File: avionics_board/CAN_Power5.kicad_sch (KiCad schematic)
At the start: 4 parts, among them U10 AP3602AKTR-G1

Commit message: create Common global libraries for footprints and symbols
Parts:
- U10: footprint SOT-23-6_DIO -> Package_TO_SOT_SMD:SOT-23-6_Handsoldering
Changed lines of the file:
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@@
 			)
 		)
-		(property "Footprint" "SOT-23-6_DIO"
+		(property "Footprint" "Package_TO_SOT_SMD:SOT-23-6_Handsoldering"
 			(at 139.065 95.25 0)
 			(effects

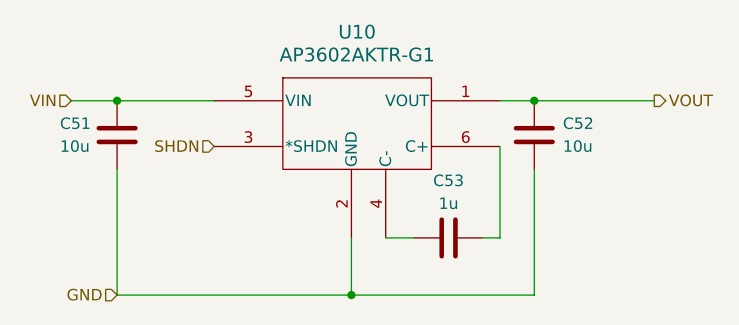
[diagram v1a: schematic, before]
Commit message: push PC104 bus reorder (no more 5V, 20 lines of 3V3 and 4 switched batt) to system components
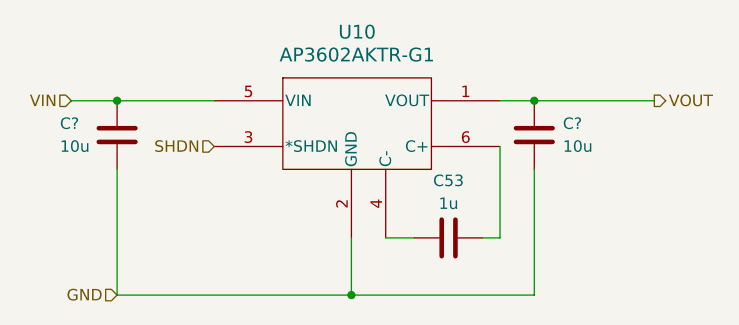
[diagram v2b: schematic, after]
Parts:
- renumbered C51 to C?, C52 to C?
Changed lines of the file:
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@@
 			(project ""
 				(path "/f6cc00ab-17f1-4973-862f-7ac95fe70668/00000000-0000-0000-0000-00005ea31c93/c43e73ca-9c1e-4d37-880f-a2757d61b5eb"
-					(reference "C52")
+					(reference "C54")
 					(unit 1)
 				)
@@
 		(on_board yes)
 		(dnp no)
-		(property "Reference" "C51"
+		(property "Reference" "C?"
 			(at 121.92 97.79 0)
 			(effects
@@
 		)
 		(instances
-			(project "sci_board"
+			(project "openlst-hw"
 				(path "/a863a5ec-a5d4-4f54-be53-e8c01d5e3ac4/53f12969-e593-459a-9671-cc23a5a9aea0/9886b2ec-bcf1-45d3-b809-b13147854a63"
-					(reference "C51")
+					(reference "C?")
 					(unit 1)
 				)
@@
 			(project "AVIONICS_BOARD"
 				(path "/f6cc00ab-17f1-4973-862f-7ac95fe70668/00000000-0000-0000-0000-00005ea31c93/c43e73ca-9c1e-4d37-880f-a2757d61b5eb"
-					(reference "C50")
+					(reference "C52")
 					(unit 1)
 				)
@@
 		(dnp no)
 		(fields_autoplaced yes)
-		(property "Reference" "C52"
+		(property "Reference" "C?"
 			(at 177.8 97.7899 0)
 			(effects
@@
 		)
 		(instances
-			(project "sci_board"
+			(project "openlst-hw"
 				(path "/a863a5ec-a5d4-4f54-be53-e8c01d5e3ac4/53f12969-e593-459a-9671-cc23a5a9aea0/9886b2ec-bcf1-45d3-b809-b13147854a63"
-					(reference "C52")
+					(reference "C?")
 					(unit 1)
 				)
@@
 			(project "AVIONICS_BOARD"
 				(path "/f6cc00ab-17f1-4973-862f-7ac95fe70668/00000000-0000-0000-0000-00005ea31c93/c43e73ca-9c1e-4d37-880f-a2757d61b5eb"
-					(reference "C51")
-					(unit 1)
-				)
+					(reference "C53")
+					(unit 1)
+				)

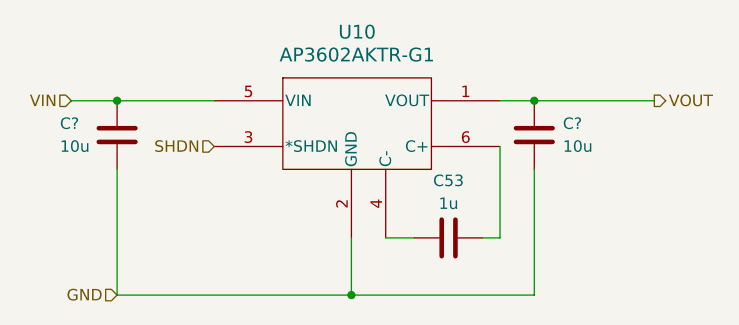
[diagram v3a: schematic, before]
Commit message: assign can power to core powerm will need to use GPIO to enable power stndby from MCUs, finalize pc104 bus assignments
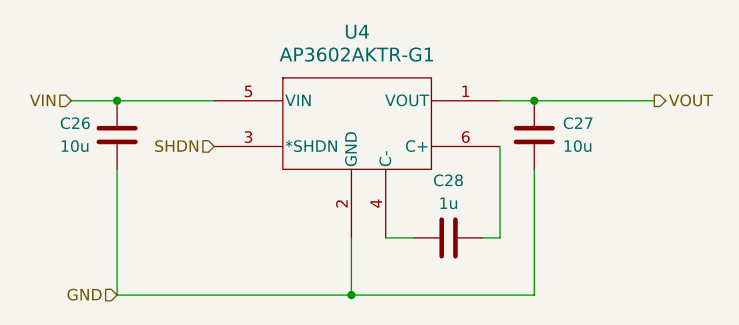
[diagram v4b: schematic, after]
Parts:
- gave numbers to parts that had none: 2
- renumbered C53 to C28, U10 to U4
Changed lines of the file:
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@@
 		(on_board yes)
 		(dnp no)
-		(property "Reference" "C53"
+		(property "Reference" "C28"
 			(at 165.1 104.14 90)
 			(effects
@@
 		)
 		(instances
-			(project ""
-				(path "/a863a5ec-a5d4-4f54-be53-e8c01d5e3ac4/53f12969-e593-459a-9671-cc23a5a9aea0/9886b2ec-bcf1-45d3-b809-b13147854a63"
-					(reference "C53")
-					(unit 1)
-				)
-			)
-			(project ""
+			(project "sci_board"
 				(path "/b4b2c88d-f6cd-4e60-862d-e21f68728580/6cda4f26-4bfa-410a-8807-c465392c7a5e"
 					(reference "C28")
@@
 				(path "/f6cc00ab-17f1-4973-862f-7ac95fe70668/00000000-0000-0000-0000-00005ea31c93/c43e73ca-9c1e-4d37-880f-a2757d61b5eb"
 					(reference "C54")
+					(unit 1)
+				)
+				(path "/f6cc00ab-17f1-4973-862f-7ac95fe70668/00000000-0000-0000-0000-00005ea31c93/00000000-0000-0000-0000-00005eab1057/c7f59f71-76ca-408f-9d9f-2fe019860d6e"
+					(reference "C62")
 					(unit 1)
 				)
@@
 		(on_board yes)
 		(dnp no)
-		(property "Reference" "C?"
+		(property "Reference" "C26"
 			(at 121.92 97.79 0)
 			(effects
@@
 		)
 		(instances
-			(project "openlst-hw"
-				(path "/a863a5ec-a5d4-4f54-be53-e8c01d5e3ac4/53f12969-e593-459a-9671-cc23a5a9aea0/9886b2ec-bcf1-45d3-b809-b13147854a63"
-					(reference "C?")
-					(unit 1)
-				)
-			)
 			(project "sci_board"
 				(path "/b4b2c88d-f6cd-4e60-862d-e21f68728580/6cda4f26-4bfa-410a-8807-c465392c7a5e"
@@
 				(path "/f6cc00ab-17f1-4973-862f-7ac95fe70668/00000000-0000-0000-0000-00005ea31c93/c43e73ca-9c1e-4d37-880f-a2757d61b5eb"
 					(reference "C52")
+					(unit 1)
+				)
+				(path "/f6cc00ab-17f1-4973-862f-7ac95fe70668/00000000-0000-0000-0000-00005ea31c93/00000000-0000-0000-0000-00005eab1057/c7f59f71-76ca-408f-9d9f-2fe019860d6e"
+					(reference "C60")
 					(unit 1)
 				)
@@
 		(dnp no)
 		(fields_autoplaced yes)
-		(property "Reference" "U10"
+		(property "Reference" "U4"
 			(at 154.94 87.63 0)
 			(effects
@@
 		)
 		(instances
-			(project ""
-				(path "/a863a5ec-a5d4-4f54-be53-e8c01d5e3ac4/53f12969-e593-459a-9671-cc23a5a9aea0/9886b2ec-bcf1-45d3-b809-b13147854a63"
-					(reference "U10")
-					(unit 1)
-				)
-			)
-			(project ""
+			(project "sci_board"
 				(path "/b4b2c88d-f6cd-4e60-862d-e21f68728580/6cda4f26-4bfa-410a-8807-c465392c7a5e"
 					(reference "U4")
@@
 				(path "/f6cc00ab-17f1-4973-862f-7ac95fe70668/00000000-0000-0000-0000-00005ea31c93/c43e73ca-9c1e-4d37-880f-a2757d61b5eb"
 					(reference "U13")
+					(unit 1)
+				)
+				(path "/f6cc00ab-17f1-4973-862f-7ac95fe70668/00000000-0000-0000-0000-00005ea31c93/00000000-0000-0000-0000-00005eab1057/c7f59f71-76ca-408f-9d9f-2fe019860d6e"
+					(reference "U18")
 					(unit 1)
 				)
@@
 		(dnp no)
 		(fields_autoplaced yes)
-		(property "Reference" "C?"
+		(property "Reference" "C27"
 			(at 177.8 97.7899 0)
 			(effects
@@
 		)
 		(instances
-			(project "openlst-hw"
-				(path "/a863a5ec-a5d4-4f54-be53-e8c01d5e3ac4/53f12969-e593-459a-9671-cc23a5a9aea0/9886b2ec-bcf1-45d3-b809-b13147854a63"
-					(reference "C?")
-					(unit 1)
-				)
-			)
 			(project "sci_board"
 				(path "/b4b2c88d-f6cd-4e60-862d-e21f68728580/6cda4f26-4bfa-410a-8807-c465392c7a5e"
@@
 					(unit 1)
 				)
+				(path "/f6cc00ab-17f1-4973-862f-7ac95fe70668/00000000-0000-0000-0000-00005ea31c93/00000000-0000-0000-0000-00005eab1057/c7f59f71-76ca-408f-9d9f-2fe019860d6e"
+					(reference "C61")
+					(unit 1)
+				)

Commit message: openlst board
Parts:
- renumbered C26 to C51, C27 to C52, C28 to C53, U4 to U10
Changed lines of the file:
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@@
 		(on_board yes)
 		(dnp no)
-		(property "Reference" "C28"
+		(property "Reference" "C53"
 			(at 165.1 104.14 90)
 			(effects
@@
 		)
 		(instances
+			(project "openlst-hw"
+				(path "/a863a5ec-a5d4-4f54-be53-e8c01d5e3ac4/53f12969-e593-459a-9671-cc23a5a9aea0/9886b2ec-bcf1-45d3-b809-b13147854a63"
+					(reference "C53")
+					(unit 1)
+				)
+			)
 			(project "sci_board"
 				(path "/b4b2c88d-f6cd-4e60-862d-e21f68728580/6cda4f26-4bfa-410a-8807-c465392c7a5e"
@@
 		(on_board yes)
 		(dnp no)
-		(property "Reference" "C26"
+		(property "Reference" "C51"
 			(at 121.92 97.79 0)
 			(effects
@@
 		)
 		(instances
+			(project "openlst-hw"
+				(path "/a863a5ec-a5d4-4f54-be53-e8c01d5e3ac4/53f12969-e593-459a-9671-cc23a5a9aea0/9886b2ec-bcf1-45d3-b809-b13147854a63"
+					(reference "C51")
+					(unit 1)
+				)
+			)
 			(project "sci_board"
 				(path "/b4b2c88d-f6cd-4e60-862d-e21f68728580/6cda4f26-4bfa-410a-8807-c465392c7a5e"
@@
 		(dnp no)
 		(fields_autoplaced yes)
-		(property "Reference" "U4"
+		(property "Reference" "U10"
 			(at 154.94 87.63 0)
 			(effects
@@
 		)
 		(instances
+			(project "openlst-hw"
+				(path "/a863a5ec-a5d4-4f54-be53-e8c01d5e3ac4/53f12969-e593-459a-9671-cc23a5a9aea0/9886b2ec-bcf1-45d3-b809-b13147854a63"
+					(reference "U10")
+					(unit 1)
+				)
+			)
 			(project "sci_board"
 				(path "/b4b2c88d-f6cd-4e60-862d-e21f68728580/6cda4f26-4bfa-410a-8807-c465392c7a5e"
@@
 		(dnp no)
 		(fields_autoplaced yes)
-		(property "Reference" "C27"
+		(property "Reference" "C52"
 			(at 177.8 97.7899 0)
 			(effects
@@
 		)
 		(instances
+			(project "openlst-hw"
+				(path "/a863a5ec-a5d4-4f54-be53-e8c01d5e3ac4/53f12969-e593-459a-9671-cc23a5a9aea0/9886b2ec-bcf1-45d3-b809-b13147854a63"
+					(reference "C52")
+					(unit 1)
+				)
+			)
 			(project "sci_board"
 				(path "/b4b2c88d-f6cd-4e60-862d-e21f68728580/6cda4f26-4bfa-410a-8807-c465392c7a5e"

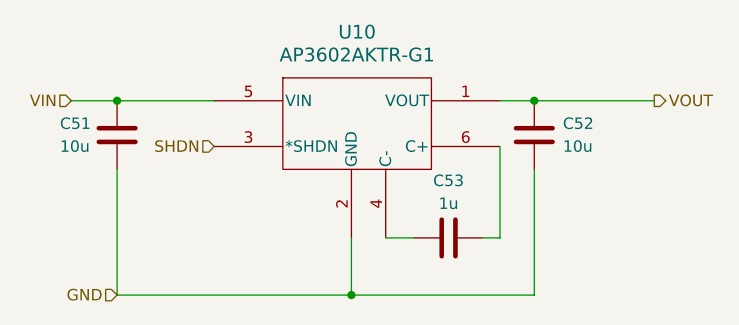
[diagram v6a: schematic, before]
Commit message: refactor AVI into nicer hierarchical components
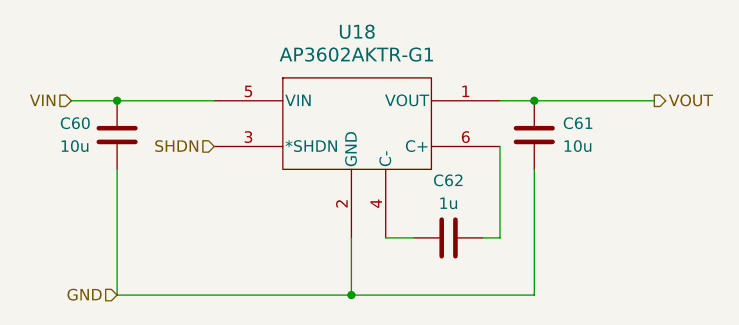
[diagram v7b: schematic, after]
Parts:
- renumbered C51 to C60, C52 to C61, C53 to C62, U10 to U18
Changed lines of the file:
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@@
 		(on_board yes)
 		(dnp no)
-		(property "Reference" "C53"
+		(property "Reference" "C62"
 			(at 165.1 104.14 90)
 			(effects
@@
 		)
 		(instances
-			(project "openlst-hw"
-				(path "/a863a5ec-a5d4-4f54-be53-e8c01d5e3ac4/53f12969-e593-459a-9671-cc23a5a9aea0/9886b2ec-bcf1-45d3-b809-b13147854a63"
-					(reference "C53")
-					(unit 1)
-				)
-			)
-			(project "sci_board"
-				(path "/b4b2c88d-f6cd-4e60-862d-e21f68728580/6cda4f26-4bfa-410a-8807-c465392c7a5e"
-					(reference "C28")
-					(unit 1)
-				)
-			)
-			(project ""
-				(path "/f6cc00ab-17f1-4973-862f-7ac95fe70668/00000000-0000-0000-0000-00005ea31c93/00000000-0000-0000-0000-00005eab1057/c7f59f71-76ca-408f-9d9f-2fe019860d6e"
+			(project "AVIONICS_BOARD"
+				(path "/f6cc00ab-17f1-4973-862f-7ac95fe70668/5de22591-2293-4710-b038-9e93720cba0f/c7f59f71-76ca-408f-9d9f-2fe019860d6e"
 					(reference "C62")
 					(unit 1)
@@
 		(on_board yes)
 		(dnp no)
-		(property "Reference" "C51"
+		(property "Reference" "C60"
 			(at 121.92 97.79 0)
 			(effects
@@
 		)
 		(instances
-			(project "openlst-hw"
-				(path "/a863a5ec-a5d4-4f54-be53-e8c01d5e3ac4/53f12969-e593-459a-9671-cc23a5a9aea0/9886b2ec-bcf1-45d3-b809-b13147854a63"
-					(reference "C51")
-					(unit 1)
-				)
-			)
-			(project "sci_board"
-				(path "/b4b2c88d-f6cd-4e60-862d-e21f68728580/6cda4f26-4bfa-410a-8807-c465392c7a5e"
-					(reference "C26")
-					(unit 1)
-				)
-			)
-			(project "AVIONICS_BOARD"
-				(path "/f6cc00ab-17f1-4973-862f-7ac95fe70668/00000000-0000-0000-0000-00005ea31c93/00000000-0000-0000-0000-00005eab1057/c7f59f71-76ca-408f-9d9f-2fe019860d6e"
+			(project "AVIONICS_BOARD"
+				(path "/f6cc00ab-17f1-4973-862f-7ac95fe70668/5de22591-2293-4710-b038-9e93720cba0f/c7f59f71-76ca-408f-9d9f-2fe019860d6e"
 					(reference "C60")
 					(unit 1)
@@
 		(dnp no)
 		(fields_autoplaced yes)
-		(property "Reference" "U10"
+		(property "Reference" "U18"
 			(at 154.94 87.63 0)
 			(effects
@@
 		)
 		(instances
-			(project "openlst-hw"
-				(path "/a863a5ec-a5d4-4f54-be53-e8c01d5e3ac4/53f12969-e593-459a-9671-cc23a5a9aea0/9886b2ec-bcf1-45d3-b809-b13147854a63"
-					(reference "U10")
-					(unit 1)
-				)
-			)
-			(project "sci_board"
-				(path "/b4b2c88d-f6cd-4e60-862d-e21f68728580/6cda4f26-4bfa-410a-8807-c465392c7a5e"
-					(reference "U4")
-					(unit 1)
-				)
-			)
-			(project ""
-				(path "/f6cc00ab-17f1-4973-862f-7ac95fe70668/00000000-0000-0000-0000-00005ea31c93/00000000-0000-0000-0000-00005eab1057/c7f59f71-76ca-408f-9d9f-2fe019860d6e"
+			(project "AVIONICS_BOARD"
+				(path "/f6cc00ab-17f1-4973-862f-7ac95fe70668/5de22591-2293-4710-b038-9e93720cba0f/c7f59f71-76ca-408f-9d9f-2fe019860d6e"
 					(reference "U18")
 					(unit 1)
@@
 		(dnp no)
 		(fields_autoplaced yes)
-		(property "Reference" "C52"
+		(property "Reference" "C61"
 			(at 177.8 97.7899 0)
 			(effects
@@
 		)
 		(instances
-			(project "openlst-hw"
-				(path "/a863a5ec-a5d4-4f54-be53-e8c01d5e3ac4/53f12969-e593-459a-9671-cc23a5a9aea0/9886b2ec-bcf1-45d3-b809-b13147854a63"
-					(reference "C52")
-					(unit 1)
-				)
-			)
-			(project "sci_board"
-				(path "/b4b2c88d-f6cd-4e60-862d-e21f68728580/6cda4f26-4bfa-410a-8807-c465392c7a5e"
-					(reference "C27")
-					(unit 1)
-				)
-			)
-			(project "AVIONICS_BOARD"
-				(path "/f6cc00ab-17f1-4973-862f-7ac95fe70668/00000000-0000-0000-0000-00005ea31c93/00000000-0000-0000-0000-00005eab1057/c7f59f71-76ca-408f-9d9f-2fe019860d6e"
+			(project "AVIONICS_BOARD"
+				(path "/f6cc00ab-17f1-4973-862f-7ac95fe70668/5de22591-2293-4710-b038-9e93720cba0f/c7f59f71-76ca-408f-9d9f-2fe019860d6e"
 					(reference "C61")
 					(unit 1)

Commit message: reconcile BOMS for AVI. SCI and AUX
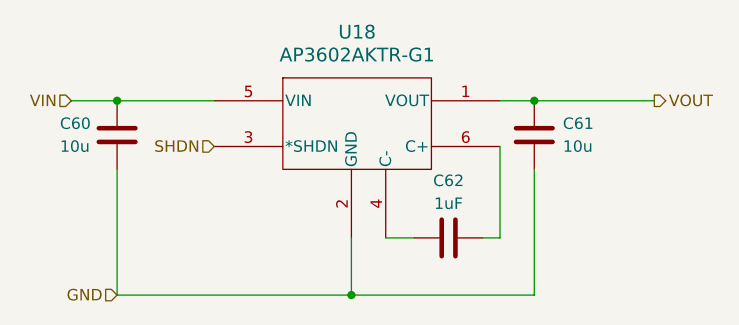
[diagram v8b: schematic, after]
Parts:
- C60, C61: Manufacturer (none) -> Murata; Part Number (none) -> GRM188R61E106KA73D; Tolerance (none) -> 10; Voltage (none) -> 25
- C62: value 1u -> 1uF; Manufacturer (none) -> Murata; Part Number (none) -> GRM188R61C105KA12D; Tolerance (none) -> 10; Voltage (none) -> 16
- U18: Manufacturer (none) -> Diodes; Part Number (none) -> AP3602AKTR-G1
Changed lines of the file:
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@@
 			)
 		)
-		(property "Value" "1u"
+		(property "Value" "1uF"
 			(at 165.1 106.68 90)
 			(effects
@@
 			)
 		)
-		(property "Datasheet" "~"
+		(property "Datasheet" "https://search.murata.co.jp/Ceramy/image/img/A01X/G101/ENG/GRM188R61C105KA12-01.pdf"
 			(at 165.1 110.49 0)
 			(effects
@@
 		)
 		(property "Alt" ""
+			(at 165.1 110.49 0)
+			(effects
+				(font
+					(size 1.27 1.27)
+				)
+				(hide yes)
+			)
+		)
+		(property "Manufacturer" "Murata"
+			(at 165.1 110.49 0)
+			(effects
+				(font
+					(size 1.27 1.27)
+				)
+				(hide yes)
+			)
+		)
+		(property "Part Number" "GRM188R61C105KA12D"
+			(at 165.1 110.49 0)
+			(effects
+				(font
+					(size 1.27 1.27)
+				)
+				(hide yes)
+			)
+		)
+		(property "Tolerance" "10"
+			(at 165.1 110.49 0)
+			(effects
+				(font
+					(size 1.27 1.27)
+				)
+				(hide yes)
+			)
+		)
+		(property "Voltage" "16"
 			(at 165.1 110.49 0)
 			(effects
@@
 			)
 		)
-		(property "Datasheet" "~"
+		(property "Datasheet" "https://search.murata.co.jp/Ceramy/image/img/A01X/G101/ENG/GRM188R61E106KA73-01.pdf"
 			(at 128.27 99.06 0)
 			(effects
@@
 		)
 		(property "Alt" ""
+			(at 128.27 99.06 0)
+			(effects
+				(font
+					(size 1.27 1.27)
+				)
+				(hide yes)
+			)
+		)
+		(property "Manufacturer" "Murata"
+			(at 128.27 99.06 0)
+			(effects
+				(font
+					(size 1.27 1.27)
+				)
+				(hide yes)
+			)
+		)
+		(property "Part Number" "GRM188R61E106KA73D"
+			(at 128.27 99.06 0)
+			(effects
+				(font
+					(size 1.27 1.27)
+				)
+				(hide yes)
+			)
+		)
+		(property "Tolerance" "10"
+			(at 128.27 99.06 0)
+			(effects
+				(font
+					(size 1.27 1.27)
+				)
+				(hide yes)
+			)
+		)
+		(property "Voltage" "25"
 			(at 128.27 99.06 0)
 			(effects
@@
 			)
 		)
-		(property "Datasheet" "AP3602AKTR-G1"
+		(property "Datasheet" "https://mm.digikey.com/Volume0/opasdata/d220001/medias/docus/503/AP3602A_B.pdf"
 			(at 139.065 95.25 0)
 			(effects
@@
 		)
 		(property "Alt" ""
+			(at 139.065 95.25 0)
+			(effects
+				(font
+					(size 1.27 1.27)
+				)
+				(hide yes)
+			)
+		)
+		(property "Manufacturer" "Diodes"
+			(at 139.065 95.25 0)
+			(effects
+				(font
+					(size 1.27 1.27)
+				)
+				(hide yes)
+			)
+		)
+		(property "Part Number" "AP3602AKTR-G1"
 			(at 139.065 95.25 0)
 			(effects
@@
 			)
 		)
-		(property "Datasheet" "~"
+		(property "Datasheet" "https://search.murata.co.jp/Ceramy/image/img/A01X/G101/ENG/GRM188R61E106KA73-01.pdf"
 			(at 174.625 99.06 0)
 			(effects
@@
 			(at 174.625 99.06 0)
 			(effects
+				(font
+					(size 1.27 1.27)
+				)
+				(hide yes)
+			)
+		)
+		(property "Manufacturer" "Murata"
+			(at 174.625 99.06 0)
+			(effects
+				(font
+					(size 1.27 1.27)
+				)
+				(hide yes)
+			)
+		)
+		(property "Part Number" "GRM188R61E106KA73D"
+			(at 174.625 99.06 0)
+			(effects
+				(font
+					(size 1.27 1.27)
+				)
+				(hide yes)
+			)
+		)
+		(property "Tolerance" "10"
+			(at 174.625 99.06 0)
+			(effects
+				(font
+					(size 1.27 1.27)
+				)
+				(hide yes)
+			)
+		)
+		(property "Voltage" "25"
+			(at 174.625 99.06 0)
+			(effects
